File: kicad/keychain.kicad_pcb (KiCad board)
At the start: 2 copper layers, 68.1 x 37.9 mm, 60 parts, among them J1 USB-C, J2 LiPo, J3 FPC-SMD_FH34SRJ-26S-0.5SH-50, Q1 BSS138, Q2 AO3401A, Q3 S8050, SW1 PWR, SW2 BOOT, SW3 USER, U1 ESP32-C6-MINI-1, U2 MCP73831, U3 AP2112K-3.3

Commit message: Baseline: owner re-placement before routing
Generated with [Devin](https://devin.ai)

Co-Authored-By: Devin <158243242+devin-ai-integration[bot]@users.noreply.github.com>
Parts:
- moved H1 64.4 mm to (94.1, 63.8)
- moved SW1 37.1 mm to (69.0, 33.9), turned to 180 degrees
- moved J3 36.9 mm to (32.9, 42.6), turned to 90 degrees
- moved LED2 35.6 mm to (57.4, 65.7)
- moved C9 13.4 mm to (81.2, 61.6)

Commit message: Route board: freerouting SES + direct-link fixes, GND zones F/B, 0 unrouted
Generated with [Devin](https://devin.ai)

Co-Authored-By: Devin <158243242+devin-ai-integration[bot]@users.noreply.github.com>
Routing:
- net /VBAT_SW: track 0.00 -> 143.9 mm, vias 0 -> 5
- net /USB_DP: track 0.00 -> 103.0 mm
- net GND: track 0.00 -> 101.1 mm, vias 0 -> 1
- net /VCC: track 0.00 -> 86.9 mm, vias 0 -> 4
- net +BATT: track 0.00 -> 76.6 mm, vias 0 -> 2
- net /EPD_VGL: track 0.00 -> 59.5 mm
- net +3V3: track 0.00 -> 57.9 mm, vias 0 -> 1
- net /LED_C2: track 0.00 -> 57.7 mm, vias 0 -> 3
- net /EPD_DC: track 0.00 -> 56.3 mm, vias 0 -> 2
- net VBUS: track 0.00 -> 55.8 mm
- net /EPD_BUSY: track 0.00 -> 54.3 mm, vias 0 -> 2
- net /EPD_CS: track 0.00 -> 53.3 mm, vias 0 -> 2
- net /EPD_RST: track 0.00 -> 53.1 mm, vias 0 -> 2
- net /USB_DM: track 0.00 -> 52.8 mm, vias 0 -> 2
- net /EPD_TVCOM: track 0.00 -> 51.2 mm, vias 0 -> 1
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- added copper zone on B.Cu, net GND
- added copper zone on F.Cu, net GND

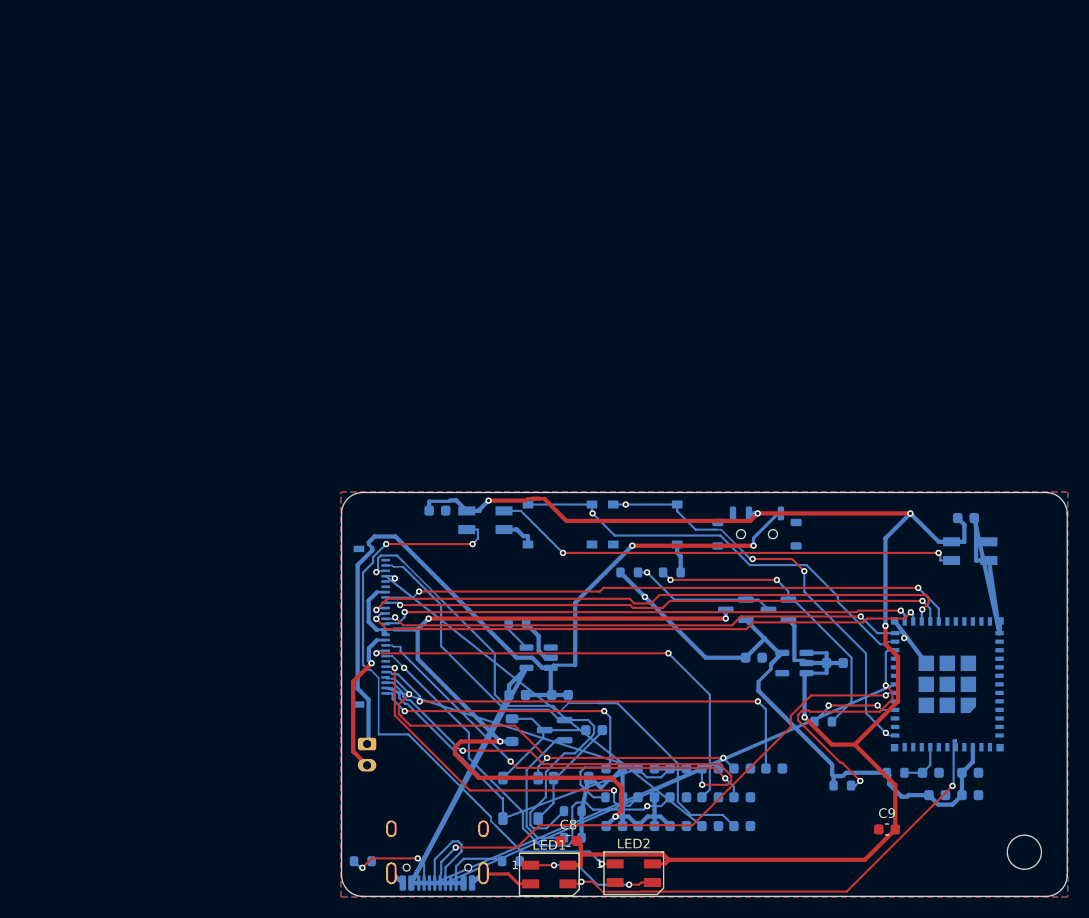
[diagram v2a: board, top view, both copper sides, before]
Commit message: Place simplified keychain board (68x38, parts on back, J1+e-paper front)
Generated with [Devin](https://devin.ai)

Co-Authored-By: Devin <158243242+devin-ai-integration[bot]@users.noreply.github.com>
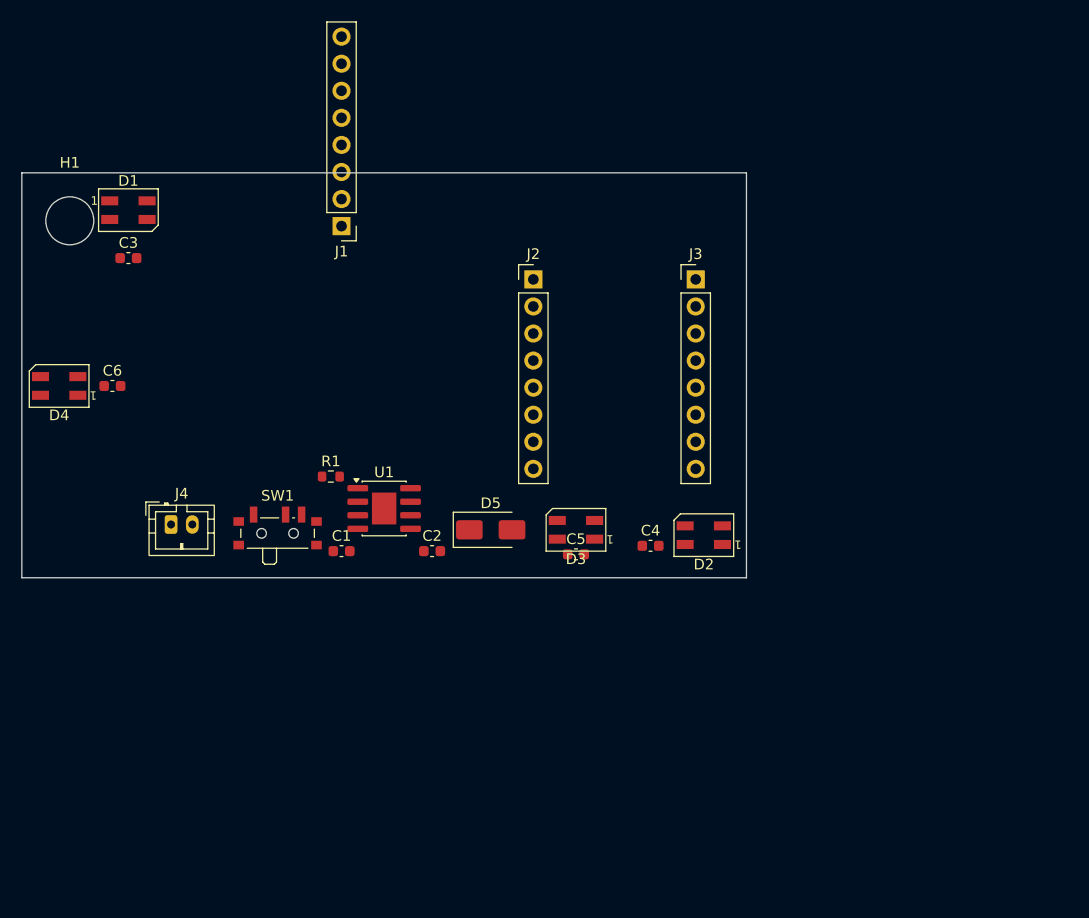
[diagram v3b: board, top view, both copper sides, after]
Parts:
- removed C10, C11, C29, C7, C8, C9: 100nF, Capacitor_SMD:C_0603_1608Metric
- removed C12, C15, C28: 4.7uF, Capacitor_SMD:C_0603_1608Metric
- removed C14, C16, C17, C18, C19, C20, C21, C22, C24, C25, C26: 1uF, Capacitor_SMD:C_0603_1608Metric
- removed C23: 1.8uF, Capacitor_SMD:C_0603_1608Metric
- removed C27: 10uF, Capacitor_SMD:C_0603_1608Metric
- removed L1: 10uH, Inductor_SMD:L_0805_2012Metric
- removed LED1, LED2, LED3, LED4: SK6812MINI, LED_SMD:LED_SK6812MINI_PLCC4_3.5x3.5mm_P1.75mm
- removed Q1: BSS138, Package_TO_SOT_SMD:SOT-23
- removed Q2: AO3401A, Package_TO_SOT_SMD:SOT-23
- removed Q3: S8050, Package_TO_SOT_SMD:SOT-23
- removed R10, R9: 47k, Resistor_SMD:R_0603_1608Metric
- removed R11, R4, R8: 10k, Resistor_SMD:R_0603_1608Metric
- removed R2: 5.1k, Resistor_SMD:R_0603_1608Metric
- removed R3: 4.7k, Resistor_SMD:R_0603_1608Metric
- removed R5: 1M, Resistor_SMD:R_0603_1608Metric
- removed R6: 0.2, Resistor_SMD:R_0603_1608Metric
- removed R7: 5M, Resistor_SMD:R_0603_1608Metric
- removed SW2: BOOT, Button_Switch_SMD:SW_Push_1P1T_XKB_TS-1187A
- removed SW3: USER, Button_Switch_SMD:SW_Push_1P1T_XKB_TS-1187A
- removed U2: MCP73831, Package_TO_SOT_SMD:SOT-23-5
- removed U3: AP2112K-3.3, Package_TO_SOT_SMD:SOT-23-5
- added D4: SK6812MINI, LED_SK6812MINI_PLCC4_3.5x3.5mm_P1.75mm, B.Cu at (3.50, 20.0)
- added D5: SS14, D_SMA, B.Cu at (44.0, 33.5)
- added J4: BATTERY, JST_PH_B2B-PH-K_1x02_P2.00mm_Vertical, B.Cu at (14.0, 33.0)
- C1, C6: footprint Capacitor_SMD:C_0603_1608Metric -> C_0603_1608Metric
- C2: value 4.7uF -> 10uF; footprint Capacitor_SMD:C_0603_1608Metric -> C_0603_1608Metric
- C3: value 1uF -> 100nF; footprint Capacitor_SMD:C_0603_1608Metric -> C_0603_1608Metric
- C4, C5: value 10uF -> 100nF; footprint Capacitor_SMD:C_0603_1608Metric -> C_0603_1608Metric
- D1, D2: value MBR0530 -> SK6812MINI; footprint Diode_SMD:D_SOD-123 -> LED_SK6812MINI_PLCC4_3.5x3.5mm_P1.75mm; moved to F.Cu
- D3: value MBR0530 -> SK6812MINI; footprint Diode_SMD:D_SOD-123 -> LED_SK6812MINI_PLCC4_3.5x3.5mm_P1.75mm
- H1: value Keyring -> MountingHole_4.5mm; footprint MountingHole:MountingHole_3.2mm_M3 -> MountingHole_4.5mm; moved to F.Cu
- J1: value USB-C -> EPAPER; footprint Connector_USB:USB_C_Receptacle_HRO_TYPE-C-31-M-12 -> PinHeader_1x08_P2.54mm_Vertical; moved to F.Cu
- J2: value LiPo -> SuperMini-L; footprint Connector_JST:JST_PH_S2B-PH-K_1x02_P2.00mm_Horizontal -> PinHeader_1x08_P2.54mm_Vertical
- J3: value FPC-SMD_FH34SRJ-26S-0.5SH-50 -> SuperMini-R; footprint Hirose_FH34SRJ-26S-0.5SH_1x26-1MP_P0.50mm_Horizontal -> PinHeader_1x08_P2.54mm_Vertical
- R1: value 5.1k -> 1.2k; footprint Resistor_SMD:R_0603_1608Metric -> R_0603_1608Metric
- SW1: value PWR -> SW_SPDT; footprint Button_Switch_SMD:SW_SPDT_Shouhan_MSK12C02 -> SW_SPDT_PCM12
- U1: value ESP32-C6-MINI-1 -> TP4056; footprint keychain:ESP32-C6-MINI-1 -> SOIC-8-1EP_3.9x4.9mm_P1.27mm_EP2.29x3mm
- moved H1 107.4 mm to (4.50, 4.50), turned to 0 degrees
- moved C6 88.3 mm to (8.50, 20.0), turned to 0 degrees
- moved C3 76.4 mm to (10.0, 8.00), turned to 0 degrees
- moved D1 64.8 mm to (10.0, 3.50), turned to 0 degrees
- moved J1 58.3 mm to (30.0, 5.00), turned to 180 degrees
- moved U1 55.4 mm to (34.0, 31.5), turned to 0 degrees
- moved J2 46.3 mm to (48.0, 10.0), turned to 0 degrees
- moved SW1 45.0 mm to (24.0, 33.5), turned to 0 degrees
- moved J3 44.5 mm to (63.2, 10.0), turned to 0 degrees
- moved C5 40.7 mm to (52.0, 35.8), turned to 0 degrees
- moved R1 36.2 mm to (29.0, 28.5), turned to 0 degrees
- moved D3 27.6 mm to (52.0, 33.5)
- moved D2 26.0 mm to (64.0, 34.0)
- moved C1 21.3 mm to (30.0, 35.5), turned to 0 degrees
- moved C2 18.1 mm to (38.5, 35.5), turned to 0 degrees
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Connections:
- C1 pad 1: GND -> +5V
- C1 pad 2: VBUS -> GND
- C2 pad 1: GND -> VBAT
- C2 pad 2: +BATT -> GND
- C3 pad 1: GND -> VBAT_SW
- C3 pad 2: /VBAT_SW -> GND
- C4 pad 1: GND -> VBAT_SW
- C4 pad 2: +3V3 -> GND
- C5 pad 1: GND -> VBAT_SW
- C5 pad 2: +3V3 -> GND
- C6 pad 1: GND -> VBAT_SW
- C6 pad 2: +3V3 -> GND
- D1 pad 1: /EPD_VGH -> D1_DO
- D1 pad 2: /EPD_LX -> GND
- D2 pad 1: GND -> D2_DO
- D2 pad 2: /EPD_CP -> GND
- D3 pad 1: /EPD_CP -> D3_DO
- D3 pad 2: /EPD_VGL -> GND
- J2 pad 1: +BATT -> +5V
- J3 pad 1: unconnected-(J3-Pin_1-Pad1) -> EPD_DC
- J3 pad 2: /EPD_GDR -> EPD_MOSI
- J3 pad 3: /EPD_TVCOM -> EPD_CS
- J3 pad 4: /EPD_1V8 -> (no net)
- J3 pad 5: unconnected-(J3-Pin_5-Pad5) -> (no net)
- J3 pad 6: unconnected-(J3-Pin_6-Pad6) -> EPD_RST
- J3 pad 7: /VCC -> (no net)
- J3 pad 8: /EPD_BUSY -> (no net)
- R1 pad 1: GND -> PROG
- R1 pad 2: /CC1 -> GND
- SW1 pad 1: +BATT -> VBAT_SW
- SW1 pad 2: /VBAT_SW -> VBAT
- SW1 pad 3: unconnected-(SW1-C-Pad3) -> (no net)
- U1 pad 2: GND -> PROG
- U1 pad 3: +3V3 -> GND
- U1 pad 4: unconnected-(U1-NC-Pad4) -> +5V
- U1 pad 5: /LED_DIN -> VBAT
- U1 pad 6: unconnected-(U1-IO3-Pad6) -> (no net)
- U1 pad 7: unconnected-(U1-NC-Pad7) -> (no net)
- U1 pad 8: /EN -> +5V
- U1 pad 9: unconnected-(U1-IO4-Pad9) -> GND
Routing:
- net /VBAT_SW: track 143.9 -> 0.00 mm, vias 5 -> 0
- net /USB_DP: track 103.0 -> 0.00 mm
- net GND: track 101.1 -> 0.00 mm, vias 1 -> 0
- net /VCC: track 86.9 -> 0.00 mm, vias 4 -> 0
- net +BATT: track 76.6 -> 0.00 mm, vias 2 -> 0
- net /EPD_VGL: track 59.5 -> 0.00 mm
- net +3V3: track 57.9 -> 0.00 mm, vias 1 -> 0
- net /LED_C2: track 57.7 -> 0.00 mm, vias 3 -> 0
- net /EPD_DC: track 56.3 -> 0.00 mm, vias 2 -> 0
- net VBUS: track 55.8 -> 0.00 mm
- net /EPD_BUSY: track 54.3 -> 0.00 mm, vias 2 -> 0
- net /EPD_CS: track 53.3 -> 0.00 mm, vias 2 -> 0
- net /EPD_RST: track 53.1 -> 0.00 mm, vias 2 -> 0
- net /USB_DM: track 52.8 -> 0.00 mm, vias 2 -> 0
- net /EPD_TVCOM: track 51.2 -> 0.00 mm, vias 1 -> 0
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- removed copper zone on B.Cu, net GND
- removed copper zone on F.Cu, net GND
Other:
- board size 68.1 x 37.9 mm -> 68 x 38 mm
- board text removed: "BOOT"
- board text removed: "PCB KEYCHAIN"
- board text removed: "USER"
- board text removed: "rev B - e-Paper"

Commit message: Fix placement: all pads >=1.5mm inside outline, J1 horizontal at top edge
Generated with [Devin](https://devin.ai)

Co-Authored-By: Devin <158243242+devin-ai-integration[bot]@users.noreply.github.com>
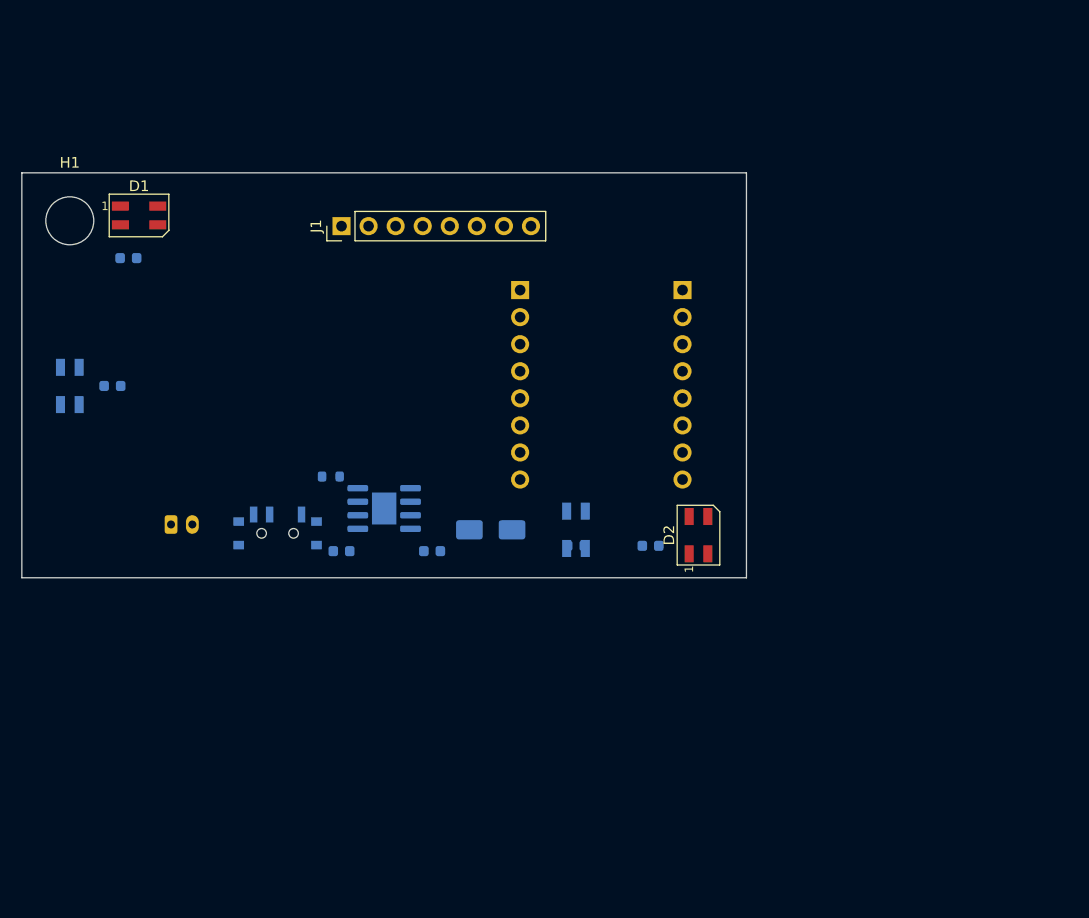
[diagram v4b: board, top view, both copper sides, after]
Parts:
- moved J2 1.59 mm to (46.8, 11.0), turned to 180 degrees
- moved J3 1.59 mm to (62.0, 11.0), turned to 180 degrees
- moved D1 1.12 mm to (11.0, 4.00)
- moved D4 1.00 mm to (4.50, 20.0), turned to 90 degrees
- moved C5 0.80 mm to (52.0, 35.0), turned to 180 degrees
- moved D2 0.50 mm to (63.5, 34.0), turned to 90 degrees
- turned C1 to 180 degrees
- turned C2 to 180 degrees
- turned C3 to 180 degrees
- turned C4 to 180 degrees
- turned C6 to 180 degrees
- turned D3 to -90 degrees
- turned D5 to 180 degrees
- turned J1 to 90 degrees
- turned R1 to 180 degrees
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
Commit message: Route board: A* router, 0 unconnected (0.3mm sig/0.5mm pwr, vias, GND zones)
Generated with [Devin](https://devin.ai)

Co-Authored-By: Devin <158243242+devin-ai-integration[bot]@users.noreply.github.com>
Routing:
- net GND: track 0.00 -> 175.9 mm, vias 0 -> 18
- net VBAT_SW: track 0.00 -> 103.8 mm, vias 0 -> 4
- net D1_DO: track 0.00 -> 86.8 mm
- net D3_DO: track 0.00 -> 62.3 mm, vias 0 -> 2
- net +5V: track 0.00 -> 55.1 mm, vias 0 -> 4
- net LED_DATA: track 0.00 -> 52.5 mm, vias 0 -> 1
- net EPD_RST: track 0.00 -> 38.1 mm
- net EPD_MOSI: track 0.00 -> 34.8 mm
- net VBAT: track 0.00 -> 33.1 mm, vias 0 -> 2
- net EPD_CS: track 0.00 -> 32.4 mm
- net +3.3V: track 0.00 -> 27.2 mm, vias 0 -> 1
- net EPD_DC: track 0.00 -> 24.7 mm
- net EPD_CLK: track 0.00 -> 22.1 mm, vias 0 -> 1
- net EPD_BUSY: track 0.00 -> 18.4 mm, vias 0 -> 1
- net PROG: track 0.00 -> 11.8 mm
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- added copper zone on B.Cu, net GND
- added copper zone on F.Cu, net GND
